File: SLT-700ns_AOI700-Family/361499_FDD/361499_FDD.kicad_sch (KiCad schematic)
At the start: 9 parts, among them U1 12-Pin_SLx_Can

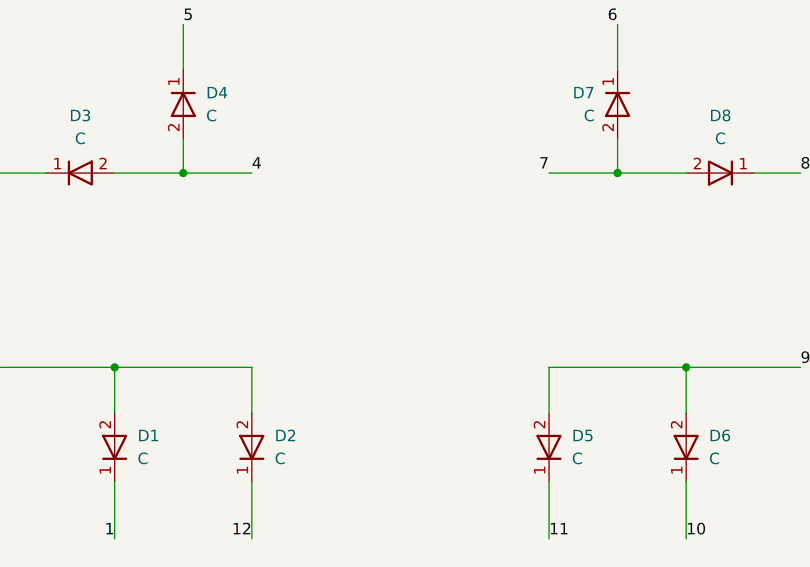
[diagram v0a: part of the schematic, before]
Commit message: Add can P/N to schematics for SLT-700
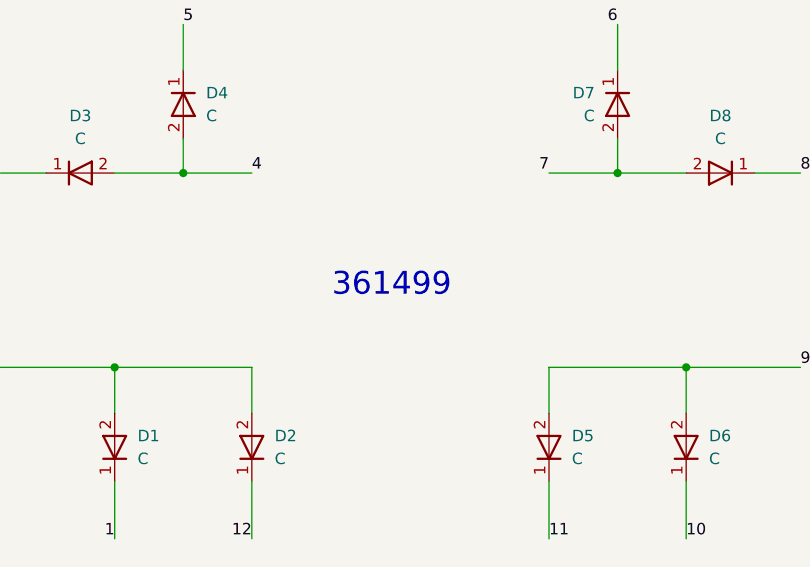
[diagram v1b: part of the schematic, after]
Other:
- note added: "361499"
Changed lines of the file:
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@@
     (effects (font (size 1.27 1.27)) (justify left bottom))
+  )
+  (text "361499" (at 113.03 93.98 0)
+    (effects (font (size 2.54 2.54)) (justify left bottom))
   )
   (label "9" (at 248.92 137.16 0)
